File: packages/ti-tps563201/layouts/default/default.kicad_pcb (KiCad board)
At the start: 2 copper layers, 12 parts

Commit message: Update picked parts and layouts for new voltage divider values
Generated by `ato build` after updating voltage divider API.

Co-Authored-By: Claude Opus 4.6 (1M context) <noreply@anthropic.com>
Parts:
- C1, C4: value 100nF ±10% 16V X7R -> 100nF ±10%
- C2, C3, C5, C6, C7: value 10µF ±10% 25V X5R -> 10µF ±10%
- L1: value 2.2µH ±20% 3.1A 42mΩ -> L 2.2µH ±20%
- R1: value 10kΩ ±1% 62.5mW -> 10kΩ ±1%
- R2: value 10kΩ ±1% 62.5mW -> 3.4kΩ ±1%; footprint UNI_ROYAL_0402WGF1002TCE:R0402 -> UNI_ROYAL_0402WGF3401TCE:R0402
- R3: value 10kΩ ±1% 62.5mW -> 4.32kΩ ±1%; footprint UNI_ROYAL_0402WGF1002TCE:R0402 -> YAGEO_AC0402FR_074K32L:R0402
- moved R3 210.4 mm to (0.00, -10.0), turned to 0 degrees
- moved R2 205.1 mm to (0.00, 0.00)
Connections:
- net SW renamed lv
- net VBST renamed hv
- net power_in-VCC renamed input_caps[2]-power-hv
- C2 pad 2: GND -> output_caps[2]-power-lv
- C3 pad 2: GND -> output_caps[2]-power-lv
- C4 pad 2: GND -> output_caps[2]-power-lv
- C5 pad 1: power-VCC -> output_caps[2]-power-hv
- C5 pad 2: GND -> output_caps[2]-power-lv
- C6 pad 1: power-VCC -> output_caps[2]-power-hv
- C6 pad 2: GND -> output_caps[2]-power-lv
- C7 pad 1: power-VCC -> output_caps[2]-power-hv
- C7 pad 2: GND -> output_caps[2]-power-lv
- L1 pad 2: power-VCC -> output_caps[2]-power-hv
- R2 pad 1: VDIV_OUTPUT -> output_caps[2]-power-hv
- R2 pad 2: GND -> ref_out-hv
- R3 pad 1: power-VCC -> ref_out-hv
- R3 pad 2: VDIV_OUTPUT -> output_caps[2]-power-lv
- U1 pad 1: GND -> output_caps[2]-power-lv
- U1 pad 4: VDIV_OUTPUT -> ref_out-hv
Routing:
- net (no net): track 0.00 -> 23.9 mm, vias 0 -> 8
- net input_caps[2]-power-hv: track 13.2 -> 0.00 mm, vias 4 -> 0
- net output_caps[2]-power-lv: track 0.00 -> 11.4 mm, vias 0 -> 7
- net GND: track 11.4 -> 0.00 mm, vias 7 -> 0
- net lv: track 4.69 -> 0.00 mm
- net VDIV_OUTPUT: track 2.38 -> 0.00 mm
- net power-VCC: track 2.33 -> 0.00 mm, vias 4 -> 0
- net hv: track 1.34 -> 0.00 mm
- added copper zone on F.Cu, net (none)
- added copper zone on F.Cu, net output_caps[2]-power-lv
- removed copper zone on F.Cu, net GND
- removed copper zone on F.Cu, net input_caps[2]-power-hv
- removed copper zone on F.Cu, net lv
- removed copper zone on F.Cu, net power-VCC

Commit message: Restore feedback divider resistor positions from pre-rename layouts
Copy the (at X Y angle) coordinates from the old r_top/r_bottom
footprints to the new chain.resistors[0]/chain.resistors[1] footprints
so board layouts are preserved.

Co-Authored-By: Claude Opus 4.6 (1M context) <noreply@anthropic.com>
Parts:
- moved R3 209.9 mm to (181.3, 95.9)
- moved R2 205.5 mm to (181.3, 96.8), turned to 180 degrees
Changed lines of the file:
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@@
 	(footprint "UNI_ROYAL_0402WGF3401TCE:R0402"
 		(layer "F.Cu")
-		(at 0 0 0)
+		(at 181.26 96.82 180)
 		(property "Reference" "R2"
 			(at -1.04 0 0)
@@
 		)
 		(property "Value" "3.4kΩ ±1%"
-			(at 0 4)
+			(at 0 4 0)
 			(layer "F.Fab")
 			(effects
@@
 		)
 		(pad "2" smd rect
-			(at 0.43 0 0)
+			(at 0.43 0 180)
 			(size 0.57 0.54)
 			(layers "F.Cu" "F.Paste" "F.Mask")
@@
 		)
 		(pad "1" smd rect
-			(at -0.43 0 0)
+			(at -0.43 0 180)
 			(size 0.57 0.54)
 			(layers "F.Cu" "F.Paste" "F.Mask")
@@
 	(footprint "YAGEO_AC0402FR_074K32L:R0402"
 		(layer "F.Cu")
-		(at 0 -10 0)
+		(at 181.27 95.86)
 		(property "Reference" "R3"
 			(at -1.04 0 0)

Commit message: Regenerate parts and fix deprecated APIs for 8 packages
- Delete auto-picked resistors/capacitors across all 8 packages
- Regenerate IC, inductor, and diode parts with fresh checksums
  (fixes is_auto_generated checksum mismatch from pragma removal)
- Replace deprecated has_single_electric_reference_shared with
  has_single_electric_reference
- Rename gnd_only parameter to ground_only
- Fix _package suffix mismatches in ti-tps54560x imports
- Replace bridge connect operators with explicit pin connections
  for raw component parts in ti-tps54560x

Packages: ti-tps82130, ti-tpsm863257, ti-lv2842x, ti-tps563201,
ti-tps54560x, st-ldk220, ti-tlv75901, ti-tps63020

Co-Authored-By: Claude Opus 4.6 (1M context) <noreply@anthropic.com>
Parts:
- R2: value 3.4kΩ ±1% -> 20kΩ ±1%; footprint UNI_ROYAL_0402WGF3401TCE:R0402 -> UNI_ROYAL_0402WGF2002TCE:R0402
- R3: value 4.32kΩ ±1% -> 25.5kΩ ±1%; footprint YAGEO_AC0402FR_074K32L:R0402 -> FOJAN_FRC0402F2552TS:R0402
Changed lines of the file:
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@@
 			)
 		)
-		(property "Datasheet" "https://lcsc.com/datasheet/lcsc_datasheet_2304241919_TI-TPS563201DDCR_C116592.pdf"
+		(property "Datasheet" "https://www.lcsc.com/datasheet/lcsc_datasheet_2304241919_Texas-Instruments-TPS563201DDCR_C116592.pdf"
 			(at 0 0 0)
 			(layer "User.9")
@@
 			)
 			(layer "F.SilkS")
+			(layers "F.SilkS")
+			(locked no)
 		)
 		(fp_line
@@
 			)
 			(layer "F.SilkS")
+			(layers "F.SilkS")
+			(locked no)
 		)
 		(fp_circle
@@
 				(type solid)
 			)
-			(fill no)
-			(layer "F.SilkS")
+			(layer "F.SilkS")
+			(locked no)
 		)
 		(fp_circle
@@
 				(type solid)
 			)
-			(fill no)
 			(layer "Cmts.User")
+			(locked no)
 		)
 		(fp_circle
@@
 				(type solid)
 			)
-			(fill no)
-			(layer "F.Fab")
+			(layer "F.Fab")
+			(locked no)
 		)
 		(pad "1" smd rect
@@
 			(net 10 "hv")
 		)
+		(embedded_fonts no)
 		(model "${KIPRJMOD}/../../parts/Texas_Instruments_TPS563201DDCR/SOT-23-6_L2.9-W1.6-H1.5-LS2.8-P0.95.step"
 			(offset
-				(xyz 0 0 0)
+				(xyz 0 0 -0)
 			)
 			(scale
@@
 		)
 	)
-	(footprint "UNI_ROYAL_0402WGF3401TCE:R0402"
+	(footprint "UNI_ROYAL_0402WGF2002TCE:R0402"
 		(layer "F.Cu")
 		(at 181.26 96.82 180)
@@
 			)
 		)
-		(property "Value" "3.4kΩ ±1%"
+		(property "Value" "20kΩ ±1%"
 			(at 0 4 0)
 			(layer "F.Fab")
@@
 			)
 		)
-		(property "LCSC" "C4940"
+		(property "LCSC" "C25765"
 			(at 0 0 0)
 			(layer "User.9")
@@
 			(hide yes)
 		)
-		(property "PARAM_resistance" "{\"type\": \"Quantity_Interval_Disjoint\", \"data\": {\"intervals\": {\"type\": \"Numeric_Interval_Disjoint\", \"data\": {\"intervals\": [{\"type\": \"Numeric_Interval\", \"data\": {\"min\": 3366.000000759959, \"max\": 3433.999999240041}}]}}, \"unit\": \"ohm\"}}"
-			(at 0 0 0)
-			(layer "User.9")
-			(hide yes)
-		)
-		(property "Partnumber" "0402WGF3401TCE"
-			(at 0 0 0)
-			(layer "User.9")
-			(hide yes)
-		)
-		(property "Datasheet" "https://www.lcsc.com/datasheet/lcsc_datasheet_2206010216_UNI-ROYAL-Uniroyal-Elec-0402WGF3401TCE_C4940.pdf"
-			(at 0 0 0)
-			(layer "User.9")
-			(hide yes)
-		)
-		(property "resistance" "3.4kΩ ±1%"
+		(property "PARAM_resistance" "{\"type\": \"Quantity_Interval_Disjoint\", \"data\": {\"intervals\": {\"type\": \"Numeric_Interval_Disjoint\", \"data\": {\"intervals\": [{\"type\": \"Numeric_Interval\", \"data\": {\"min\": 19800.00000447035, \"max\": 20199.99999552965}}]}}, \"unit\": \"ohm\"}}"
+			(at 0 0 0)
+			(layer "User.9")
+			(hide yes)
+		)
+		(property "Partnumber" "0402WGF2002TCE"
+			(at 0 0 0)
+			(layer "User.9")
+			(hide yes)
+		)
+		(property "Datasheet" "https://www.lcsc.com/datasheet/lcsc_datasheet_2206010100_UNI-ROYAL-Uniroyal-Elec-0402WGF2002TCE_C25765.pdf"
+			(at 0 0 0)
+			(layer "User.9")
+			(hide yes)
+		)
+		(property "resistance" "20kΩ ±1%"
 			(at 0 0 0)
 			(layer "User.9")
@@
 			(hide yes)
 		)
-		(property "lcsc_id" "C4940"
+		(property "lcsc_id" "C25765"
 			(at 0 0 0)
 			(layer "User.9")
@@
 		)
 		(embedded_fonts no)
-		(model "${KIPRJMOD}/../../parts/UNI_ROYAL_0402WGF3401TCE/R0402_L1.0-W0.5-H0.4.step"
+		(model "${KIPRJMOD}/../../parts/UNI_ROYAL_0402WGF2002TCE/R0402_L1.0-W0.5-H0.4.step"
 			(offset
 				(xyz 0 0 -0)
@@
 		)
 	)
-	(footprint "YAGEO_AC0402FR_074K32L:R0402"
+	(footprint "FOJAN_FRC0402F2552TS:R0402"
 		(layer "F.Cu")
 		(at 181.27 95.86)
@@
 			)
 		)
-		(property "Value" "4.32kΩ ±1%"
+		(property "Value" "25.5kΩ ±1%"
 			(at 0 4)
 			(layer "F.Fab")
@@
 			)
 		)
-		(property "LCSC" "C227108"
-			(at 0 0 0)
-			(layer "User.9")
-			(hide yes)
-		)
-		(property "Manufacturer" "YAGEO"
+		(property "LCSC" "C2998160"
+			(at 0 0 0)
+			(layer "User.9")
+			(hide yes)
+		)
+		(property "Manufacturer" "FOJAN"
 			(at 0 0 0)
 			(layer "User.9")
@@
 			(hide yes)
 		)
-		(property "PARAM_resistance" "{\"type\": \"Quantity_Interval_Disjoint\", \"data\": {\"intervals\": {\"type\": \"Numeric_Interval_Disjoint\", \"data\": {\"intervals\": [{\"type\": \"Numeric_Interval\", \"data\": {\"min\": 4276.800000965595, \"max\": 4363.199999034405}}]}}, \"unit\": \"ohm\"}}"
-			(at 0 0 0)
-			(layer "User.9")
-			(hide yes)
-		)
-		(property "Partnumber" "AC0402FR-074K32L"
-			(at 0 0 0)
-			(layer "User.9")
-			(hide yes)
-		)
-		(property "Datasheet" "https://www.lcsc.com/datasheet/lcsc_datasheet_1912111437_YAGEO-AC0402FR-074K32L_C227108.pdf"
-			(at 0 0 0)
-			(layer "User.9")
-			(hide yes)
-		)
-		(property "resistance" "4.32kΩ ±1%"
+		(property "PARAM_resistance" "{\"type\": \"Quantity_Interval_Disjoint\", \"data\": {\"intervals\": {\"type\": \"Numeric_Interval_Disjoint\", \"data\": {\"intervals\": [{\"type\": \"Numeric_Interval\", \"data\": {\"min\": 25245.000005699694, \"max\": 25754.999994300306}}]}}, \"unit\": \"ohm\"}}"
+			(at 0 0 0)
+			(layer "User.9")
+			(hide yes)
+		)
+		(property "Partnumber" "FRC0402F2552TS"
+			(at 0 0 0)
+			(layer "User.9")
+			(hide yes)
+		)
+		(property "Datasheet" "https://wmsc.lcsc.com/wmsc/upload/file/pdf/v2/lcsc/2308241947_FOJAN-FRC0402F2552TS_C2998160.pdf"
+			(at 0 0 0)
+			(layer "User.9")
+			(hide yes)
+		)
+		(property "resistance" "25.5kΩ ±1%"
 			(at 0 0 0)
 			(layer "User.9")
@@
 			(hide yes)
 		)
-		(property "lcsc_id" "C227108"
+		(property "lcsc_id" "C2998160"
 			(at 0 0 0)
 			(layer "User.9")
@@
 			(hide yes)
 		)
-		(attr smd)
+		(attr through_hole)
 		(fp_line
 			(start -0.23 0.5)
@@
 		)
 		(embedded_fonts no)
-		(model "${KIPRJMOD}/../../parts/YAGEO_AC0402FR_074K32L/R0402_L1.0-W0.5-H0.4.step"
+		(model "${KIPRJMOD}/../../parts/FOJAN_FRC0402F2552TS/R0402_L1.0-W0.5-H0.4.step"
 			(offset
-				(xyz 0 0 -0)
+				(xyz 0 -0 0)
 			)
 			(scale

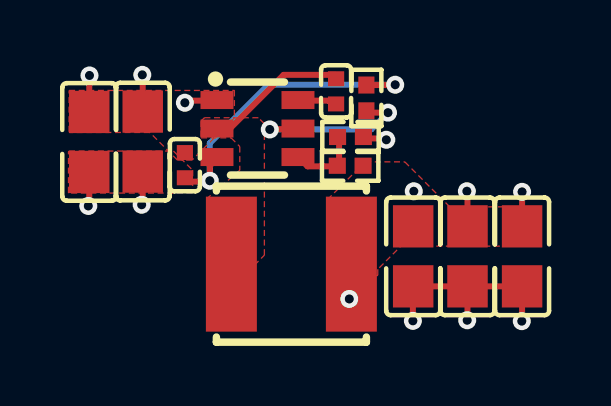
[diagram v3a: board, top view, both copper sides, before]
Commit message: Simplify ti-lv2842x usage to single regulator, rebuild layouts
- Reduce usage.ato to one 24V→3.3V regulator (avoids solver picking
  obscure resistor values with sparse EasyEDA coverage)
- Rebuild layouts for ti-lv2842x, ti-tps54560x, ti-tps563201, ti-tps63020
- Fix ti-tps82130 comment formatting (linter)

Co-Authored-By: Claude Opus 4.6 (1M context) <noreply@anthropic.com>
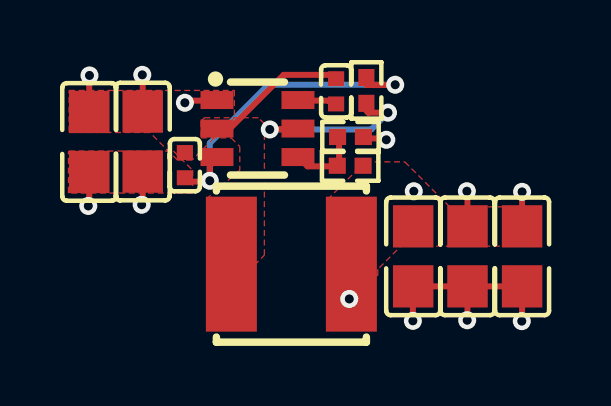
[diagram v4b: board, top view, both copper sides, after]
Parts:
- moved R1 0.25 mm to (181.8, 94.3)
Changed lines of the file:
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@@
 	(footprint "UNI_ROYAL_0402WGF1002TCE:R0402"
 		(layer "F.Cu")
-		(at 181.8 94.56 90)
+		(at 181.8 94.31 90)
 		(property "Reference" "R1"
 			(at 0 -4 0)
